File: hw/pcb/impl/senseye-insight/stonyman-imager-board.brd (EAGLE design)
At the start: 14.6 x 16.2 mm, 10 parts, among them J1 HEADER_12PIN2X6_NOSILK, U1 STONYMANDEFAULT_LENS_MOUNT, U2 TI_ADCXX1S101

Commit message: added GND trace between the caps and edge of board
The polygone for the GND plane didn't fill this in, but there was room,
and I think it belonged there
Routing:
- net GND: track 4.51 -> 9.60 mm
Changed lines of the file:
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@@
 <setting verticaltext="up"/>
 </settings>
-<grid distance="0.1" unitdist="inch" unit="inch" style="lines" multiple="1" display="yes" altdistance="0.01" altunitdist="inch" altunit="inch"/>
+<grid distance="0.1" unitdist="inch" unit="inch" style="lines" multiple="1" display="yes" altdistance="0.001" altunitdist="inch" altunit="inch"/>
 <layers>
 <layer number="1" name="Top" color="4" fill="1" visible="yes" active="yes"/>
@@
 <layer number="27" name="tValues" color="7" fill="1" visible="no" active="yes"/>
 <layer number="28" name="bValues" color="7" fill="1" visible="no" active="yes"/>
-<layer number="29" name="tStop" color="7" fill="3" visible="no" active="yes"/>
-<layer number="30" name="bStop" color="7" fill="6" visible="no" active="yes"/>
+<layer number="29" name="tStop" color="7" fill="3" visible="yes" active="yes"/>
+<layer number="30" name="bStop" color="7" fill="6" visible="yes" active="yes"/>
 <layer number="31" name="tCream" color="7" fill="4" visible="no" active="yes"/>
 <layer number="32" name="bCream" color="7" fill="5" visible="no" active="yes"/>
@@
 <via x="11.6586" y="5.6388" extent="1-16" drill="0.3556" diameter="0.254"/>
 <contactref element="C5" pad="2"/>
+<wire x1="2.9464" y1="5.3848" x2="2.6162" y2="5.715" width="0.2032" layer="16"/>
+<wire x1="2.6162" y1="5.715" x2="2.6162" y2="10.3378" width="0.2032" layer="16"/>
 </signal>
 <signal name="V_STONY">

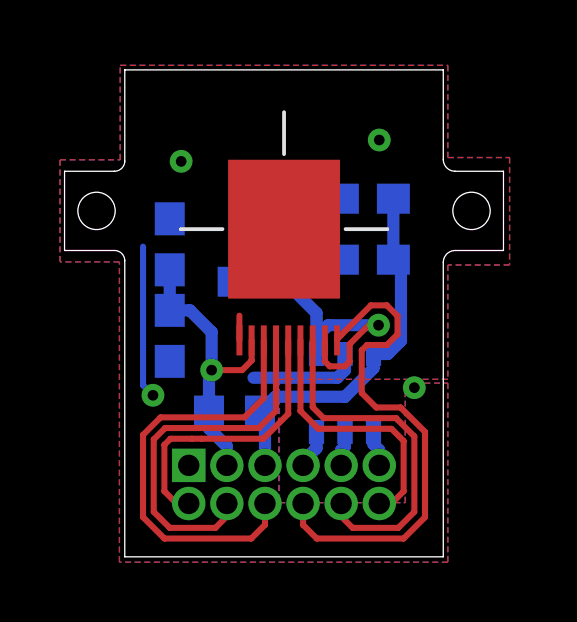
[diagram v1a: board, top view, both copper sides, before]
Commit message: updated board dimensions to accomodate lens mount
Added extra width on the tabs to give more space for the mounting
holes.  also moved everything above the 0.05 in headers up just a little
bit to give more space between headers and the lens mount.
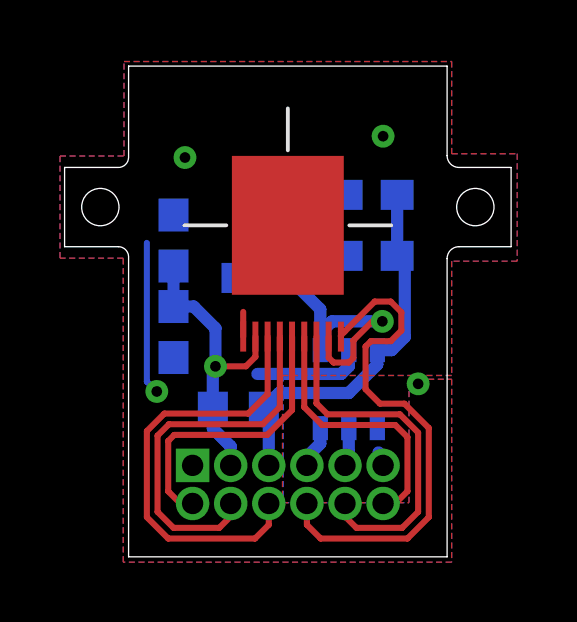
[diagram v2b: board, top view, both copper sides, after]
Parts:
- moved C5 0.18 mm to (6.63, 9.30)
- moved C1 0.18 mm to (3.63, 10.5)
- moved C2 0.18 mm to (3.63, 7.49)
- moved R1 0.18 mm to (5.79, 4.95)
- moved U$1 0.18 mm to (5.33, 13.2)
- moved C3 0.18 mm to (10.2, 12.1)
- moved C4 0.18 mm to (10.2, 10.0)
- moved U1 0.18 mm to (7.44, 11.0)
- moved U2 0.18 mm to (9.47, 5.59)
- moved J1 0.13 mm to (7.44, 2.41)
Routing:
- net ADC-SCLK: track 1.19 -> 0.49 mm
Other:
- board size 14.6 x 16.2 mm -> 14.9 x 16.4 mm

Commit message: added more space between headers and lens mount
now the tDocu layers of the headers and the lens mount do not overlap at
all.
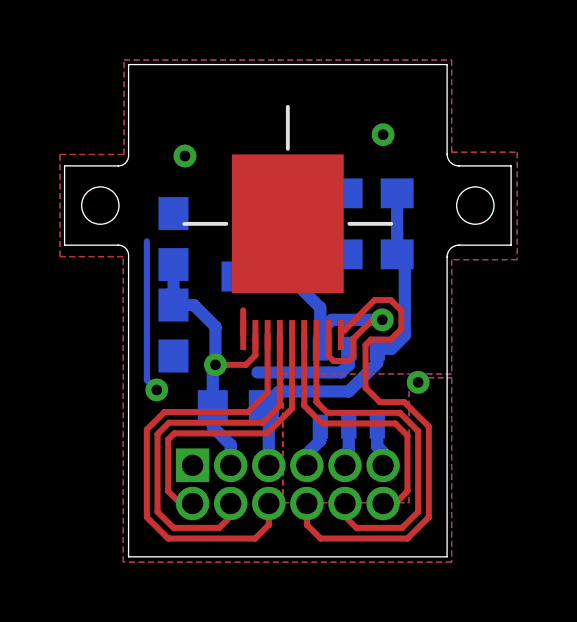
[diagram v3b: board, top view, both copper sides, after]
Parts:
- moved C3 0.05 mm to (10.2, 12.1)
- moved C4 0.05 mm to (10.2, 10.1)
- moved C5 0.05 mm to (6.63, 9.35)
- moved U$1 0.05 mm to (5.33, 13.3)
- moved U1 0.05 mm to (7.44, 11.1)
- moved C2 0.05 mm to (3.63, 7.54)
- moved R1 0.05 mm to (5.79, 5.00)
- moved U2 0.05 mm to (9.47, 5.64)
- moved C1 0.05 mm to (3.63, 10.6)
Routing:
- net ADC-SCLK: track 0.49 -> 1.37 mm
